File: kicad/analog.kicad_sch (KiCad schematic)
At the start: 23 parts, among them J26 ADC #1 in 2, J27 ADC #1 in 3, J36 ADC #1 in 0, J37 ADC #1 in 1, U5 ADS1115IDGSR

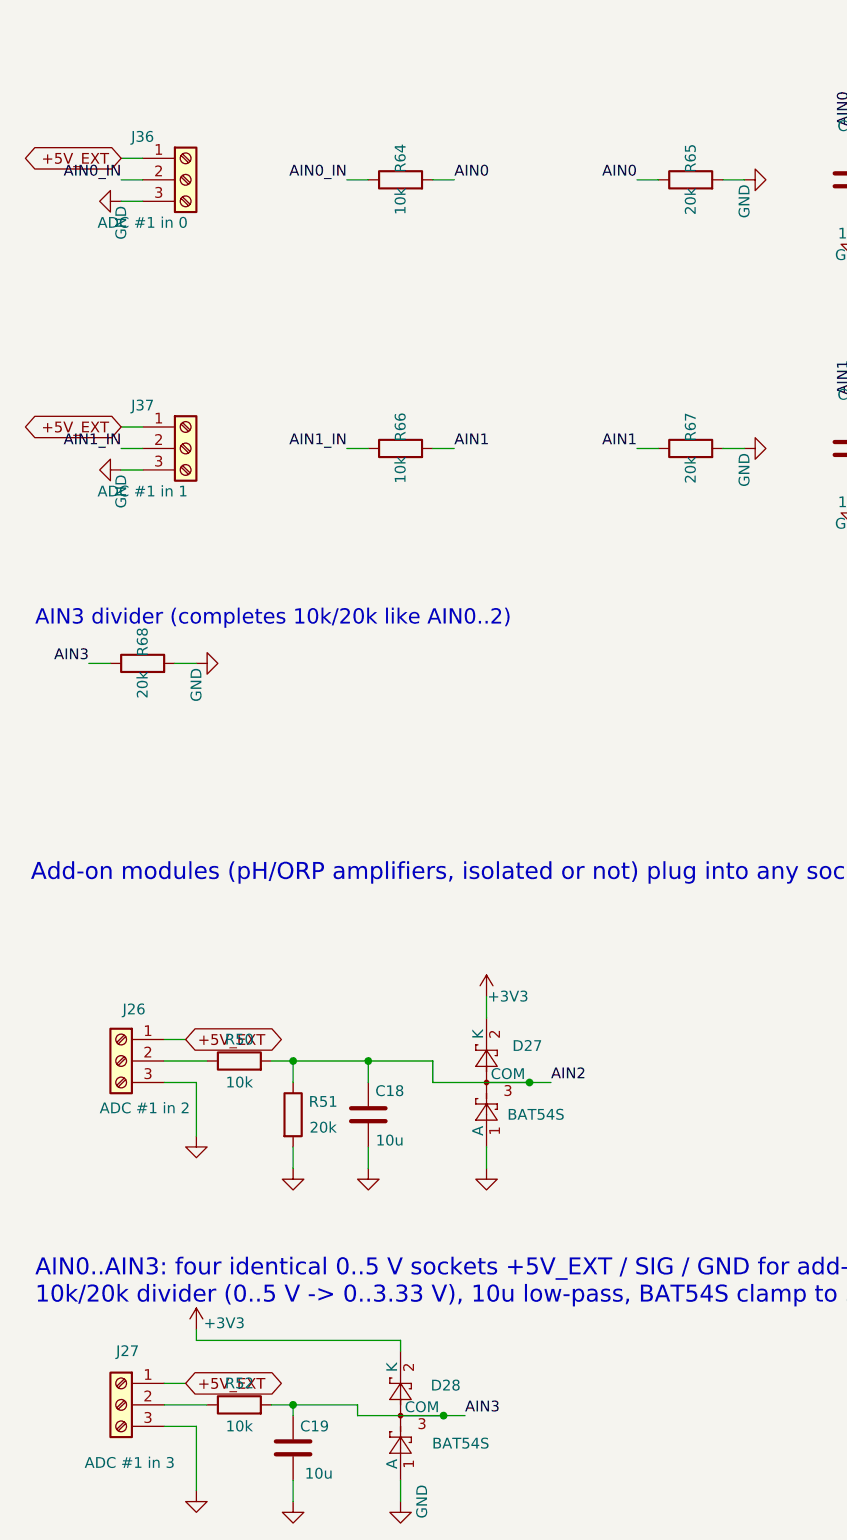
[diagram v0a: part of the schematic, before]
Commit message: kicad: pin headers for 1-Wire, ADC and floats; connectivity-driven re-placement
J19, ADC sockets (J36/J37/J26/J27, 3x4 grid) and floats J30/J31 are pin headers now. All footprints placed on the board (big connectors first, flat parts allowed under the Pi, user-placed U10/RN5/J32/U11 and user routing kept): signal ratsnest 7824 -> 4450 mm, crossings 1776 -> 862. ERC 0, DRC copper 0, parity 0.

Co-Authored-By: Claude Opus 5.5 <noreply@anthropic.com>
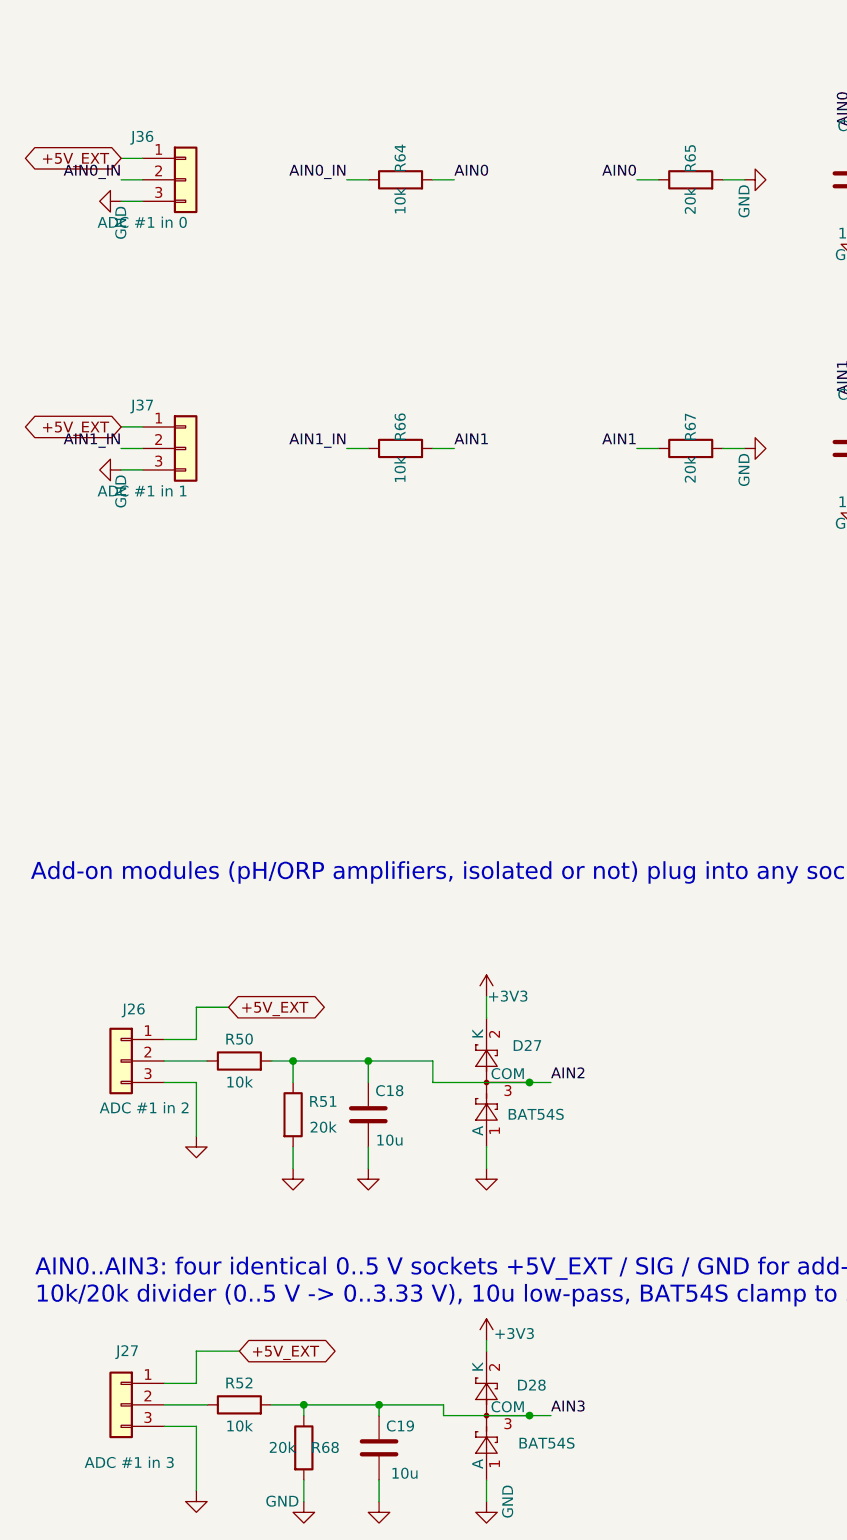
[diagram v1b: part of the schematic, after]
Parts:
- J26, J27: footprint aquaPCB:TerminalBlock_Kangnex_WJ250B-3.5-03P_P3.50mm_Staggered -> Connector_PinHeader_2.54mm:PinHeader_1x03_P2.54mm_Vertical; symbol Connector:Screw_Terminal_01x03 -> Connector_Generic:Conn_01x03; KiLib_Generator terminal_block/Phoenix -> connector/pin_header_socket; LCSC C8420 -> (none)
- J36, J37: footprint aquaPCB:TerminalBlock_Kangnex_WJ250B-3.5-03P_P3.50mm_Staggered -> Connector_PinHeader_2.54mm:PinHeader_1x03_P2.54mm_Vertical; symbol Connector:Screw_Terminal_01x03 -> Connector_Generic:Conn_01x03; LCSC C8420 -> (none)
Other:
- note removed: "AIN3 divider (completes 10k/20k like AIN0..2)"
- moved on the sheet: C19, D28, R68

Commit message: kicad: v2 layout finished - ADC renumbering, port labels, last routes
- ADC sockets numbered 0..3 from right to left; AIN0<->AIN1 and AIN2<->AIN3
  swapped at the ADS1115, U5 end runs re-routed.
- Connector labels: IoRegistry-style port names (PCA#1 chNN, ADC #1 in n,
  GPIO n, DS1820); J5/J6/J8/J9 corrected from GPIO to PCA#1 ch15/14/13/12
  (also in outputs.kicad_sch). Back side: names with voltage/current
  ratings, running from the board edge at pin 1, "+" on supply pins,
  SCL/SDA and 1-Wire Data marks. Front: ADC #1 / in n, jumper labels.
- Routed the last six open nets (+3V3 at J24/JP4, +5V_EXT at J19,
  GPIO2_SDA J22-J23 on B.Cu, AIN1, J24 pin 10 - JP3, PCA1_CH1); PCA1_CH3
  partly moved to B.Cu to free the corridor at U7. Dangling stubs removed.
- Silkscreen: nothing on pads, overlaps reduced with small moves; part
  references and F.Fab texts at 0.8 mm.
- aquaPCB.kicad_dru: the deliberate courtyard overlap of the ADC socket
  pairs J26/J27 and J36/J37 (2.54 mm grid) is waived by a custom rule.

ERC clean, DRC without errors (silkscreen warnings only), board fully
routed and in sync with the schematic.

Co-Authored-By: Claude Opus 5.5 <noreply@anthropic.com>
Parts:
- C27, C28: footprint Capacitor_SMD:C_0603_1608Metric -> Capacitor_SMD:C_0805_2012Metric; LCSC C19702 -> C15850
- J26: value ADC #1 in 2 -> ADC#1-3
- J27: value ADC #1 in 3 -> ADC#1-2
- J36: value ADC #1 in 0 -> ADC#1-1
- J37: value ADC #1 in 1 -> ADC#1-0
- R64, R66: footprint Resistor_SMD:R_0603_1608Metric -> Resistor_SMD:R_0805_2012Metric; LCSC C25804 -> C17414
- R65, R67, R68: footprint Resistor_SMD:R_0603_1608Metric -> Resistor_SMD:R_0805_2012Metric; LCSC C4184 -> C4328
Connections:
- net AIN0: now also C28.1, D36.3 (COM), R66.2, R67.1; no longer C27.1, D35.3 (COM), R64.2, R65.1
- net AIN0_IN: now also J37.2 (Pin_2), R66.1; no longer J36.2 (Pin_2), R64.1
- net AIN1: now also C27.1, D35.3 (COM), R64.2, R65.1; no longer C28.1, D36.3 (COM), R66.2, R67.1
- net AIN1_IN: now also J36.2 (Pin_2), R64.1; no longer J37.2 (Pin_2), R66.1
- net AIN2: now also C19.1, D28.3 (COM), R52.2, R68.1; no longer C18.1, D27.3 (COM), R50.2, R51.1
- net AIN3: now also C18.1, D27.3 (COM), R50.2, R51.1; no longer C19.1, D28.3 (COM), R52.2, R68.1
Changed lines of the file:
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@@
 		)
 	)
-	(label "AIN0_IN"
+	(label "AIN1_IN"
 		(at 62.23 101.6 180)
 		(effects
@@
 		)
 	)
-	(label "AIN2"
+	(label "AIN3"
 		(at 86.36 208.28 0)
 		(effects
@@
 		)
 	)
-	(label "AIN1_IN"
+	(label "AIN0_IN"
 		(at 62.23 133.35 180)
 		(effects
@@
 		)
 	)
-	(label "AIN3"
+	(label "AIN2"
 		(at 86.36 247.65 0)
 		(effects
@@
 		)
 	)
-	(label "AIN1"
+	(label "AIN0"
 		(at 121.92 127 90)
 		(effects
@@
 		)
 	)
-	(label "AIN0"
+	(label "AIN1"
 		(at 96.52 101.6 180)
 		(effects
@@
 		)
 	)
-	(label "AIN0"
+	(label "AIN1"
 		(at 121.92 95.25 90)
 		(effects
@@
 		)
 	)
-	(label "AIN0_IN"
+	(label "AIN1_IN"
 		(at 35.56 101.6 180)
 		(effects
@@
 		)
 	)
-	(label "AIN0"
+	(label "AIN1"
 		(at 74.93 101.6 0)
 		(effects
@@
 		)
 	)
-	(label "AIN1"
+	(label "AIN0"
 		(at 96.52 133.35 180)
 		(effects
@@
 		)
 	)
-	(label "AIN1"
+	(label "AIN0"
 		(at 74.93 133.35 0)
 		(effects
@@
 		)
 	)
-	(label "AIN1"
+	(label "AIN0"
 		(at 144.78 134.62 270)
 		(effects
@@
 		)
 	)
-	(label "AIN1_IN"
+	(label "AIN0_IN"
 		(at 35.56 133.35 180)
 		(effects
@@
 		)
 	)
-	(label "AIN0"
+	(label "AIN1"
 		(at 144.78 102.87 270)
 		(effects
@@
 			)
 		)
-		(property "Footprint" "Resistor_SMD:R_0603_1608Metric"
+		(property "Footprint" "Resistor_SMD:R_0805_2012Metric"
 			(at 102.87 133.35 0)
 			(hide yes)
@@
 			)
 		)
-		(property "LCSC" "C4184"
+		(property "LCSC" "C4328"
 			(at 102.87 133.35 0)
 			(hide yes)
@@
 			)
 		)
-		(property "Footprint" "Resistor_SMD:R_0603_1608Metric"
+		(property "Footprint" "Resistor_SMD:R_0805_2012Metric"
 			(at 102.87 101.6 0)
 			(hide yes)
@@
 			)
 		)
-		(property "LCSC" "C4184"
+		(property "LCSC" "C4328"
 			(at 102.87 101.6 0)
 			(hide yes)
@@
 			)
 		)
-		(property "Footprint" "Capacitor_SMD:C_0603_1608Metric"
+		(property "Footprint" "Capacitor_SMD:C_0805_2012Metric"
 			(at 121.92 101.6 0)
 			(hide yes)
@@
 			)
 		)
-		(property "LCSC" "C19702"
+		(property "LCSC" "C15850"
 			(at 121.92 101.6 0)
 			(hide yes)
@@
 			)
 		)
-		(property "Value" "ADC #1 in 3"
+		(property "Value" "ADC#1-2"
 			(at 36.576 253.238 0)
 			(show_name no)
@@
 			)
 		)
-		(property "Value" "ADC #1 in 0"
+		(property "Value" "ADC#1-1"
 			(at 38.1 106.68 0)
 			(show_name no)
@@
 			)
 		)
-		(property "Footprint" "Resistor_SMD:R_0603_1608Metric"
+		(property "Footprint" "Resistor_SMD:R_0805_2012Metric"
 			(at 68.58 101.6 0)
 			(hide yes)
@@
 			)
 		)
-		(property "LCSC" "C25804"
+		(property "LCSC" "C17414"
 			(at 68.58 101.6 0)
 			(hide yes)
@@
 			)
 		)
-		(property "Footprint" "Resistor_SMD:R_0603_1608Metric"
+		(property "Footprint" "Resistor_SMD:R_0805_2012Metric"
 			(at 68.58 133.35 0)
 			(hide yes)
@@
 			)
 		)
-		(property "LCSC" "C25804"
+		(property "LCSC" "C17414"
 			(at 68.58 133.35 0)
 			(hide yes)
@@
 			)
 		)
-		(property "Value" "ADC #1 in 2"
+		(property "Value" "ADC#1-3"
 			(at 38.354 211.328 0)
 			(show_name no)
@@
 			)
 		)
-		(property "Footprint" "Resistor_SMD:R_0603_1608Metric"
+		(property "Footprint" "Resistor_SMD:R_0805_2012Metric"
 			(at 57.15 251.46 0)
 			(hide yes)
@@
 			)
 		)
-		(property "LCSC" "C4184"
+		(property "LCSC" "C4328"
 			(at 57.15 251.46 0)
 			(hide yes)
@@
 			)
 		)
-		(property "Footprint" "Capacitor_SMD:C_0603_1608Metric"
+		(property "Footprint" "Capacitor_SMD:C_0805_2012Metric"
 			(at 121.92 133.35 0)
 			(hide yes)
@@
 			)
 		)
-		(property "LCSC" "C19702"
+		(property "LCSC" "C15850"
 			(at 121.92 133.35 0)
 			(hide yes)
@@
 			)
 		)
-		(property "Value" "ADC #1 in 1"
+		(property "Value" "ADC#1-0"
 			(at 38.1 138.43 0)
 			(show_name no)
